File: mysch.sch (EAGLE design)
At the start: 40 parts, among them IC1 CY8C4247LQI-BL483, IC2 74HC595N, Q1 RFD3055LE, Q2 32.768KHz, U1 HC-05

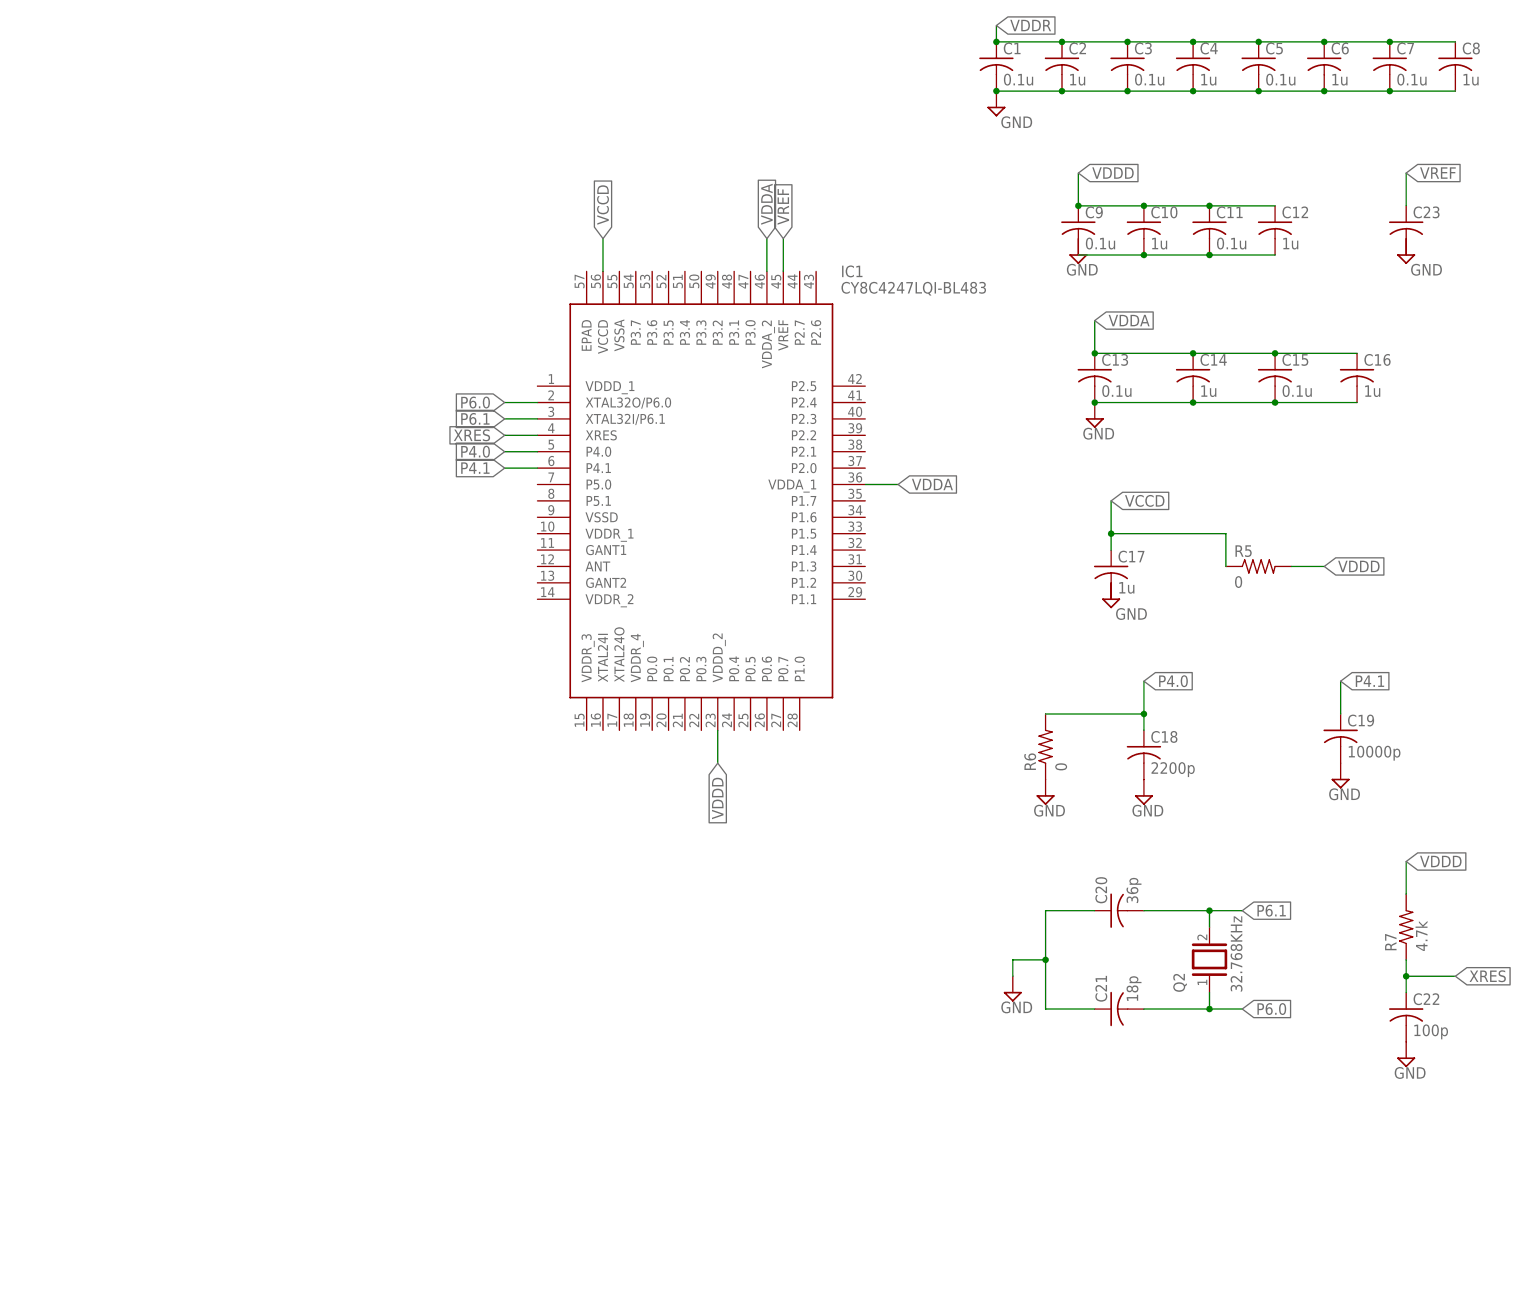
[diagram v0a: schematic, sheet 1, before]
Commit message: selected ECO and WCO
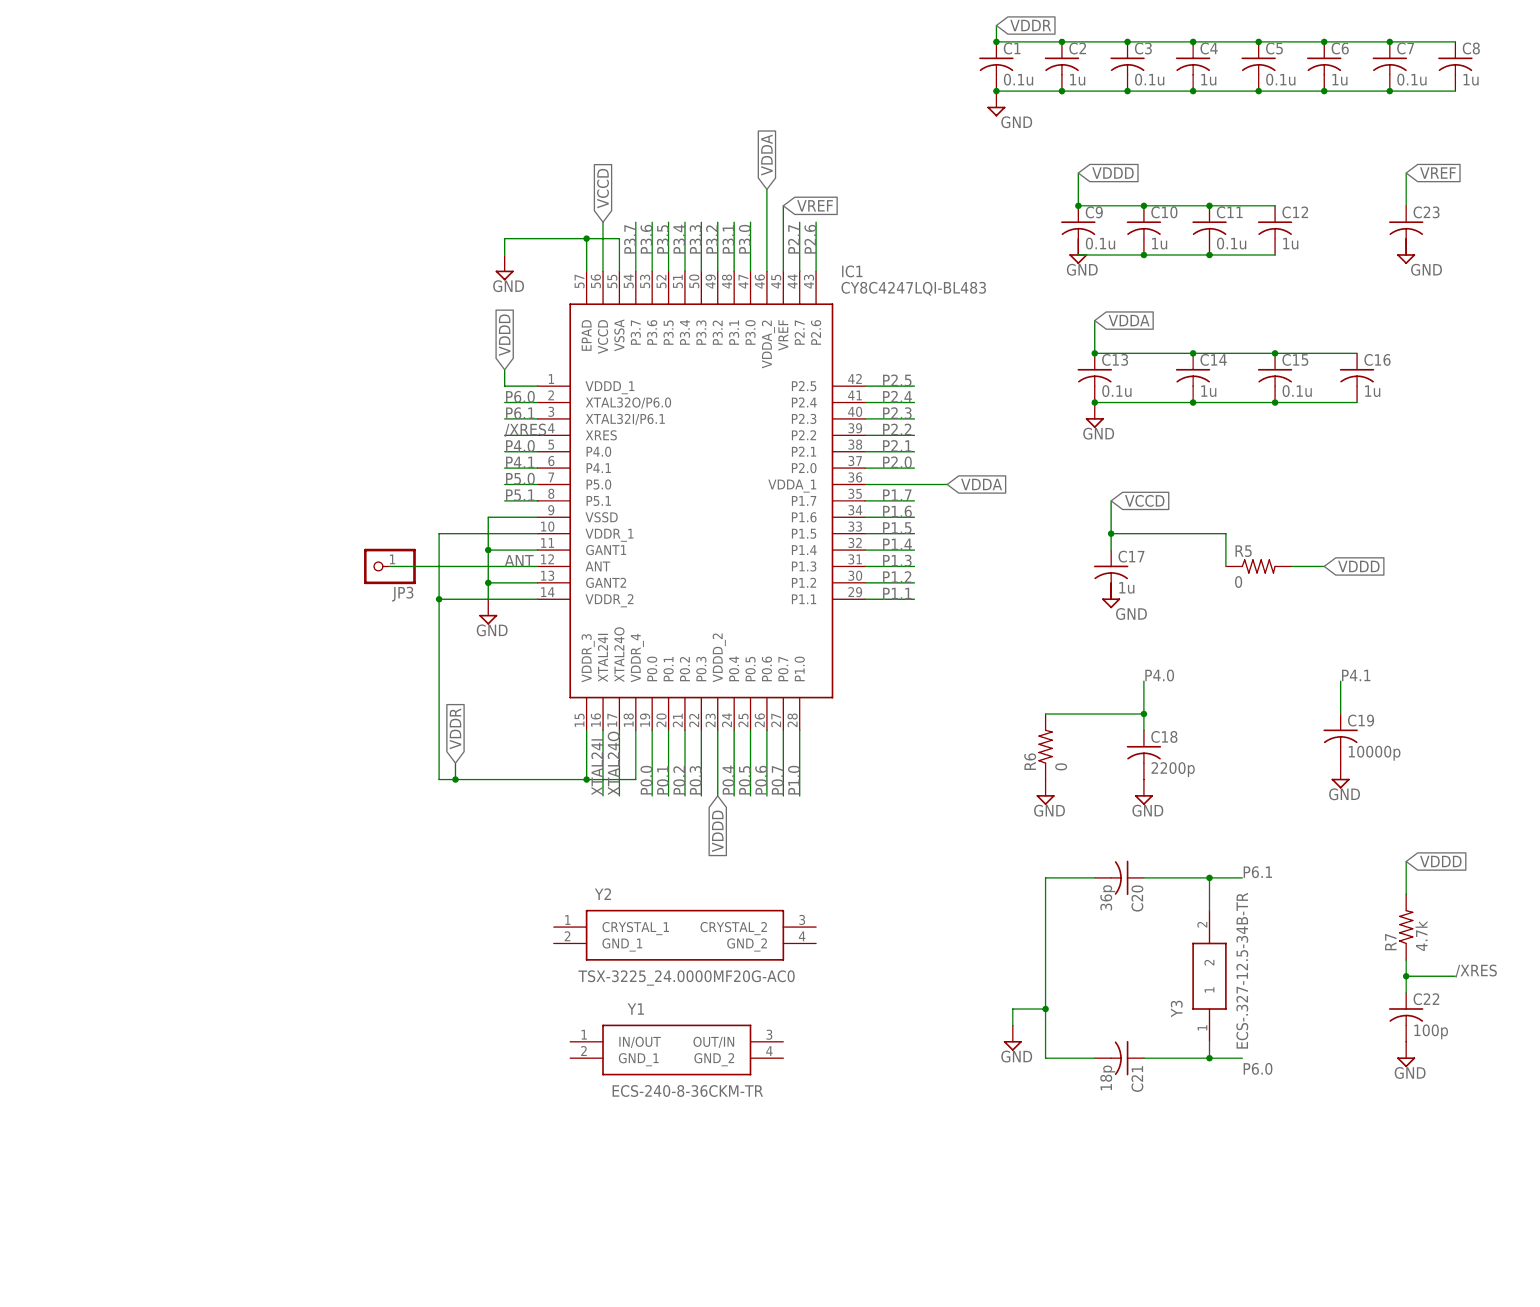
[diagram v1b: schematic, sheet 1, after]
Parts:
- removed Q2: 32.768KHz, special:XTAL/S
- added JP3: (no value), adafruit:PINHD-1X1
- added Y1: ECS-240-8-36CKM-TR, SamacSys_Parts:ECS-240-8-36CKM-TR
- added Y2: TSX-3225_24.0000MF20G-AC0, SamacSys_Parts:TSX-3225_24.0000MF20G-AC0
- added Y3: ECS-.327-12.5-34B-TR, SamacSys_Parts:ECS-.327-12.5-34B-TR
- C1, C10, C11, C12, C13, C17, C18, C19, C2, C20, C21, C22, C3, C5, C6, C7, C8: device rcl:C-USC0805K -> rcl:C-USC0805
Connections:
- net XRES renamed /XRES
- new net ANT: IC1.ANT, JP3.1
- new net P0.0: IC1.P0.0
- new net P0.1: IC1.P0.1
- new net P0.2: IC1.P0.2
- new net P0.3: IC1.P0.3
- new net P0.4: IC1.P0.4
- new net P0.5: IC1.P0.5
- new net P0.6: IC1.P0.6
- new net P0.7: IC1.P0.7
- new net P1.0: IC1.P1.0
- new net P1.1: IC1.P1.1
- new net P1.2: IC1.P1.2
- new net P1.3: IC1.P1.3
- new net P1.4: IC1.P1.4
- new net P1.5: IC1.P1.5
- new net P1.6: IC1.P1.6
- new net P1.7: IC1.P1.7
- new net P2.0: IC1.P2.0
- new net P2.1: IC1.P2.1
- new net P2.2: IC1.P2.2
- new net P2.3: IC1.P2.3
- new net P2.4: IC1.P2.4
- new net P2.5: IC1.P2.5
- new net P2.6: IC1.P2.6
- new net P2.7: IC1.P2.7
- new net P3.0: IC1.P3.0
- new net P3.1: IC1.P3.1
- new net P3.2: IC1.P3.2
- new net P3.3: IC1.P3.3
- new net P3.4: IC1.P3.4
- new net P3.5: IC1.P3.5
- new net P3.6: IC1.P3.6
- new net P3.7: IC1.P3.7
- new net P5.0: IC1.P5.0
- new net P5.1: IC1.P5.1
- new net XTAL24I: IC1.XTAL24I
- new net XTAL24O: IC1.XTAL24O
- net GND: now also C20.2, C21.2, IC1.EPAD, IC1.GANT1, IC1.GANT2, IC1.VSSA, IC1.VSSD; no longer C20.1, C21.1
- net P6.0: now also C21.1, Y3.1; no longer C21.2, Q2.1
- net P6.1: now also C20.1, Y3.2; no longer C20.2, Q2.2
- net VDDD: now also IC1.VDDD_1
- net VDDR: now also IC1.VDDR_1, IC1.VDDR_2, IC1.VDDR_3, IC1.VDDR_4
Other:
- moved on the sheet: C20, C21

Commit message: SWD modified
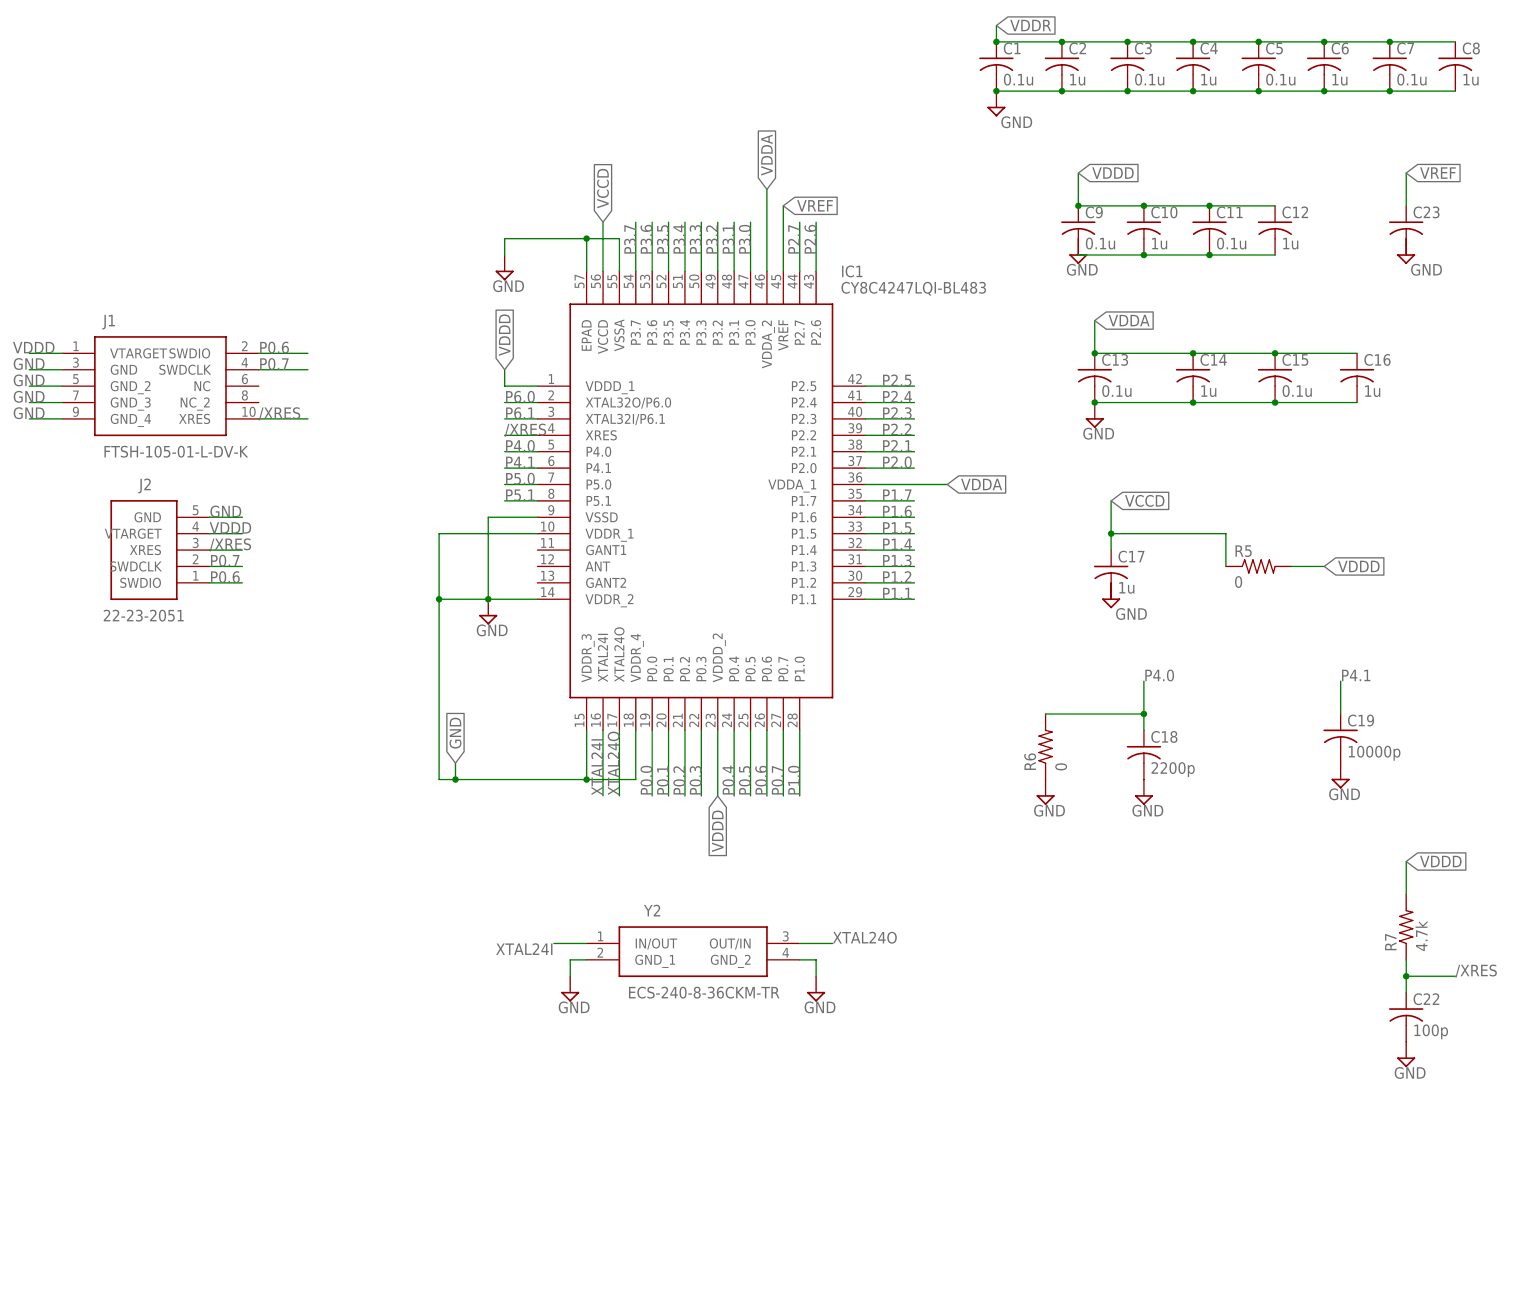
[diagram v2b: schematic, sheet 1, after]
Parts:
- removed C20: 36p, rcl:C-USC0805
- removed C21: 18p, rcl:C-USC0805
- removed JP3: (no value), adafruit:PINHD-1X1
- removed Y1: ECS-240-8-36CKM-TR, SamacSys_Parts:ECS-240-8-36CKM-TR
- removed Y3: ECS-.327-12.5-34B-TR, SamacSys_Parts:ECS-.327-12.5-34B-TR
- added J1: FTSH-105-01-L-DV-K, SamacSys_Parts:FTSH-105-01-L-DV-K
- added J2: 22-23-2051, SamacSys_Parts:22-23-2051
- added LED2: (no value), led:LEDSML0805
- BT_SLAVE: SPICEPREFIX (none) -> X
- Y2: value TSX-3225_24.0000MF20G-AC0 -> ECS-240-8-36CKM-TR; device SamacSys_Parts:TSX-3225_24.0000MF20G-AC0 -> SamacSys_Parts:ECS-240-8-36CKM-TR
- renumbered U1 to BT_SLAVE
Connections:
- net N$2 renamed KEY
- net N$6 renamed UART_RX
- removed net ANT: IC1.ANT, JP3.1
- removed net N$7: BT_SLAVE.UART-TX, JP2.1
- removed net N$9: JP1.2, R1.2
- new net N$2: LED2.A, R1.2
- new net UART_TX: BT_SLAVE.!UART-CTS, JP2.1
- net /XRES: now also J1.XRES, J2.XRES
- net GND: now also IC1.VDDR_1, IC1.VDDR_2, IC1.VDDR_3, IC1.VDDR_4, J1.GND, J1.GND_2, J1.GND_3, J1.GND_4, J2.GND, LED2.C, Y2.GND_1, Y2.GND_2; no longer C20.2, C21.2, IC1.GANT1, IC1.GANT2
- net P0.6: now also J1.SWDIO, J2.SWDIO
- net P0.7: now also J1.SWDCLK, J2.SWDCLK
- net P6.0: no longer C21.1, Y3.1
- net P6.1: no longer C20.1, Y3.2
- net VDDD: now also J1.VTARGET, J2.VTARGET
- net VDDR: no longer IC1.VDDR_1, IC1.VDDR_2, IC1.VDDR_3, IC1.VDDR_4
- net XTAL24I: now also Y2.IN/OUT
- net XTAL24O: now also Y2.OUT/IN
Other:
- moved on the sheet: JP2, Y2
